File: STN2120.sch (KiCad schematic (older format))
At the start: 28 parts

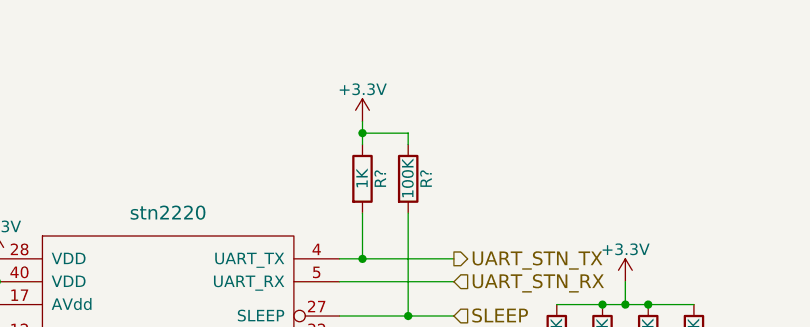
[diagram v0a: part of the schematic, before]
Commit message: added uC
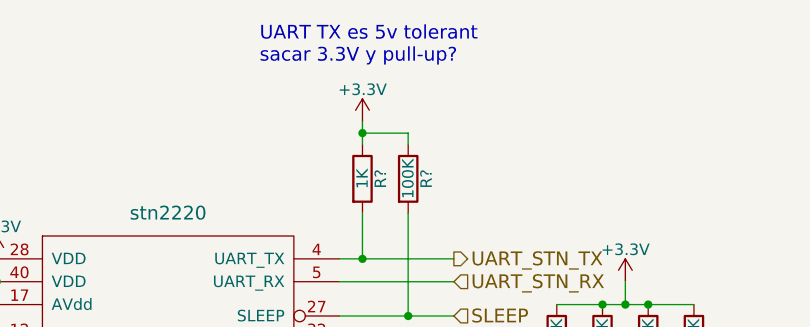
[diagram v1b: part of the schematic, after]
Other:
- note added: "UART TX es 5v tolerant\nsacar 3.3V y pull-up?"
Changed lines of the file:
@@
 LIBS:PESD1CAN
 LIBS:stn2120
+LIBS:switches
 LIBS:PF_APINER-cache
 EELAYER 25 0
@@
 $Descr A4 11693 8268
 encoding utf-8
-Sheet 7 7
+Sheet 7 8
 Title ""
 Date ""
@@
 Wire Wire Line
 	3300 5500 3300 5250
+Text Notes 5850 1600 0    60   ~ 0
+UART TX es 5v tolerant\nsacar 3.3V y pull-up?
 $EndSCHEMATC

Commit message: ready for first rev
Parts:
- removed R?: 1K, symbol R
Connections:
- net +3V3: no longer R?.1
- net +5V: now also R?.1
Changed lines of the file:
@@
 CADA UNO CERCA DE\nVDD Y AVDD
-$Comp
-L R R?
-U 1 1 5AFEF90D
-P 6300 2100
-F 0 "R?" V 6380 2100 50  0000 C CNN
-F 1 "1K" V 6300 2100 50  0000 C CNN
-F 2 "" V 6230 2100 50  0001 C CNN
-F 3 "" H 6300 2100 50  0001 C CNN
-	1    6300 2100
-	1    0    0    -1
-$EndComp
 $Comp
 L +3.3V #PWR?
 U 1 1 5AFEF9F2
-P 6300 1850
-F 0 "#PWR?" H 6300 1700 50  0001 C CNN
-F 1 "+3.3V" H 6300 1990 50  0000 C CNN
-F 2 "" H 6300 1850 50  0001 C CNN
-F 3 "" H 6300 1850 50  0001 C CNN
-	1    6300 1850
+P 6500 1900
+F 0 "#PWR?" H 6500 1750 50  0001 C CNN
+F 1 "+3.3V" H 6500 2040 50  0000 C CNN
+F 2 "" H 6500 1900 50  0001 C CNN
+F 3 "" H 6500 1900 50  0001 C CNN
+	1    6500 1900
 	1    0    0    -1
 $EndComp
@@
 Text HLabel 6700 2550 2    60   Input ~ 0
 UART_STN_RX
-Wire Wire Line
-	6300 1850 6300 1950
 Wire Wire Line
 	6200 2450 6700 2450
@@
 	4550 2500 4550 2450
 Wire Wire Line
-	4350 2450 4700 2450
-Wire Wire Line
 	4550 2800 4700 2800
 $Comp
@@
 Wire Wire Line
 	4350 2500 4350 2450
-Connection ~ 4550 2450
 Wire Wire Line
 	4350 2800 4350 2900
@@
 	1    0    0    -1
 $EndComp
-Wire Wire Line
-	6300 2250 6300 2450
-Connection ~ 6300 2450
 Text HLabel 6700 2700 2    60   Input ~ 0
 SLEEP
@@
 Connection ~ 6500 2700
 Wire Wire Line
-	6300 1900 6500 1900
-Wire Wire Line
 	6500 1900 6500 1950
-Connection ~ 6300 1900
 Text HLabel 6350 2800 2    60   Output ~ 0
 PWR_CTRL
@@
 Text Notes 5850 1600 0    60   ~ 0
 UART TX es 5v tolerant\nsacar 3.3V y pull-up?
+$Comp
+L +5V #PWR?
+U 1 1 5B06FB2A
+P 4350 2450
+F 0 "#PWR?" H 4350 2300 50  0001 C CNN
+F 1 "+5V" H 4350 2590 50  0000 C CNN
+F 2 "" H 4350 2450 50  0001 C CNN
+F 3 "" H 4350 2450 50  0001 C CNN
+	1    4350 2450
+	1    0    0    -1
+$EndComp
+Wire Wire Line
+	4550 2450 4700 2450
 $EndSCHEMATC

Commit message: fixed some ports errors
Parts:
- gave numbers to parts that had none: 27
